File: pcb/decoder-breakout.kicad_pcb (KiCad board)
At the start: 2 copper layers, 18 parts, among them J1 SM04B-SRSS-TB_LF__SN_, J2 SM04B-SRSS-TB_LF__SN_, J3 TBL009-254-08GY-2GY, Q1 BSS138, Q2 BSS138, U1 LS7866-S

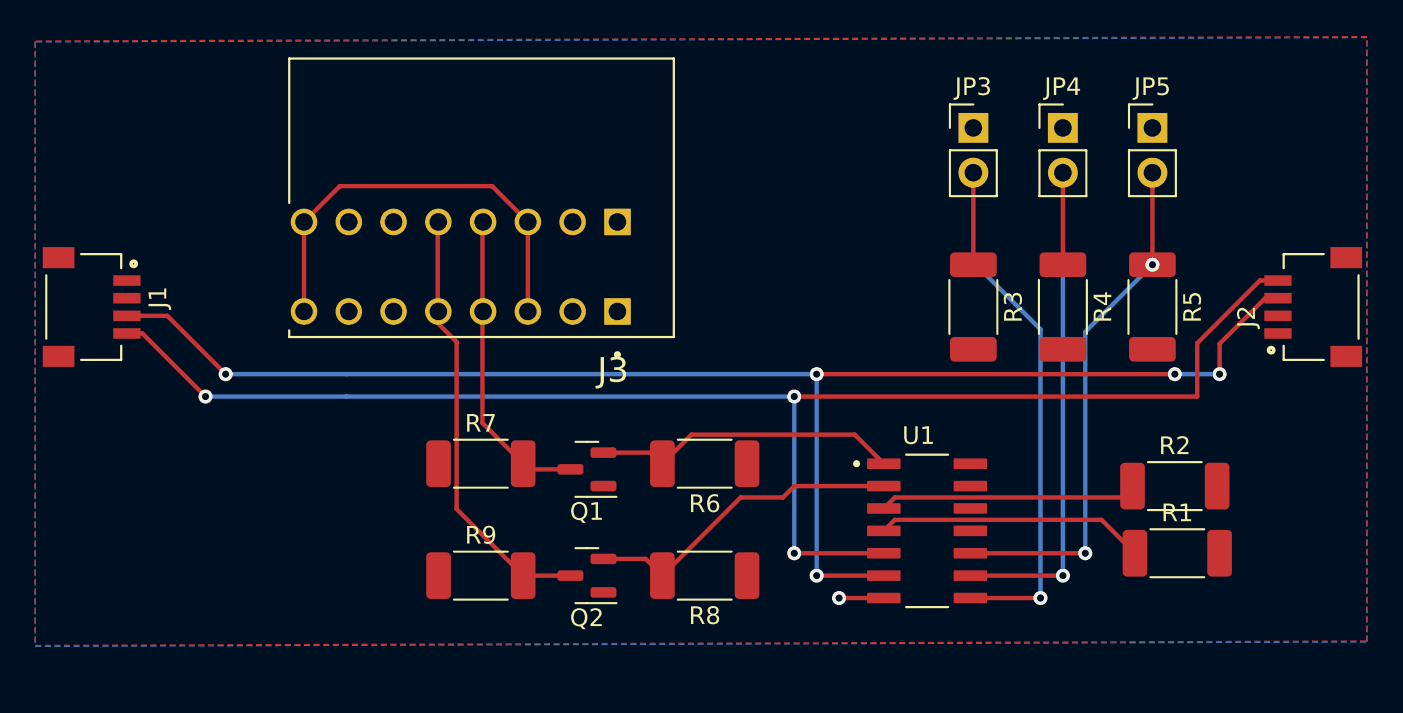
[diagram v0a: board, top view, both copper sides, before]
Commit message: add decoupling cap, mounting holes and board edges
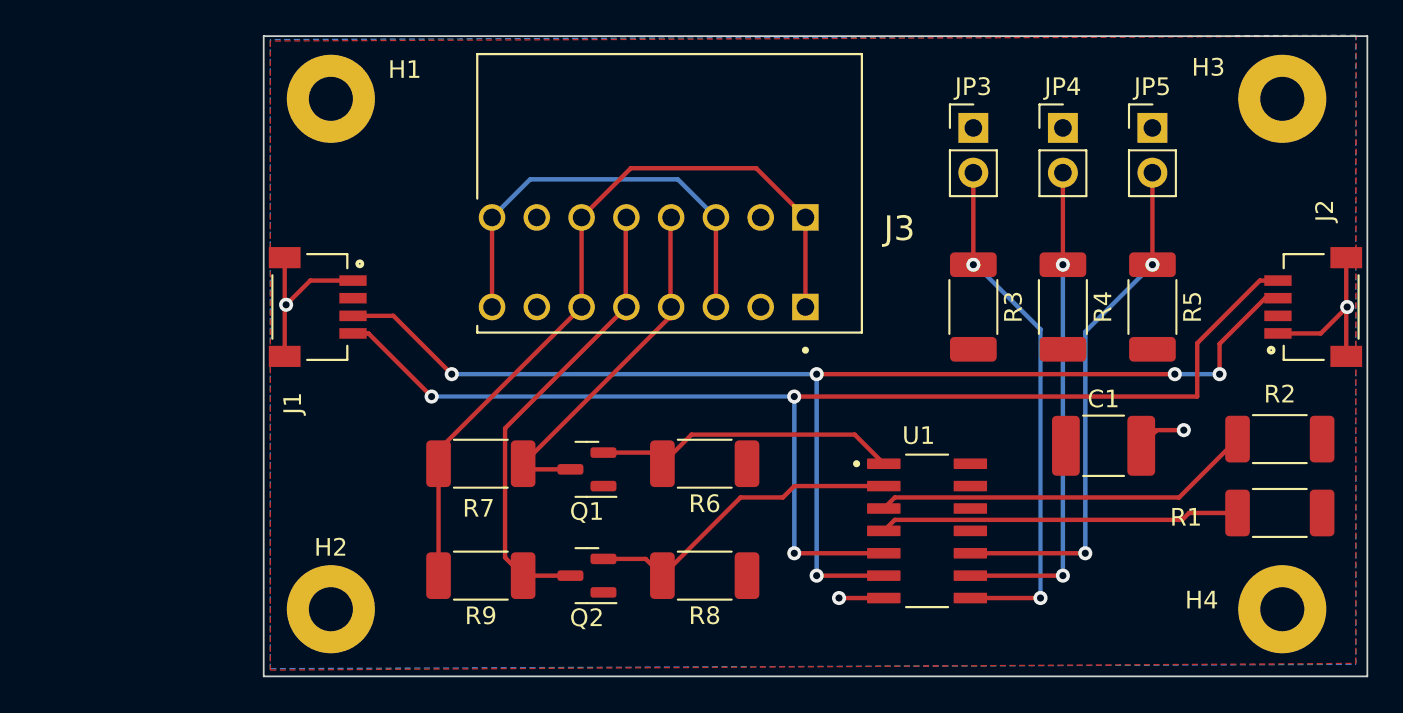
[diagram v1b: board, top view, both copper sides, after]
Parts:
- added C1: C, Capacitor_SMD:C_1812_4532Metric_Pad1.57x3.40mm_HandSolder, F.Cu at (142.0, 99.3)
- added H1: MountingHole, MountingHole:MountingHole_2.5mm_Pad, F.Cu at (98.2, 79.6)
- added H2: MountingHole, MountingHole:MountingHole_2.5mm_Pad, F.Cu at (98.2, 108.6)
- added H3: MountingHole, MountingHole:MountingHole_2.5mm_Pad, F.Cu at (152.1, 79.6)
- added H4: MountingHole, MountingHole:MountingHole_2.5mm_Pad, F.Cu at (152.1, 108.6)
- moved J1 12.8 mm to (99.4, 91.4)
- moved J3 10.7 mm to (125.1, 91.4)
- moved R2 6.53 mm to (152.0, 98.9)
- moved R1 6.25 mm to (152.0, 103.1)
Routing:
- net +5v: track 0.00 -> 43.8 mm
- net GND: track 2.54 -> 25.5 mm, vias 1 -> 4
- net Net-(U1-SDA): track 84.7 -> 71.9 mm
- net Net-(U1-SCL): track 85.3 -> 72.4 mm
- net Net-(U1-Z): track 14.6 -> 21.7 mm
- net Net-(U1-CE): track 15.3 -> 20.5 mm
- net Encoder_A: track 16.8 -> 20.3 mm
- net Encoder_B: track 24.1 -> 26.3 mm
- net Net-(JP4-B): vias 1 -> 2
- net Net-(JP3-B): vias 1 -> 2
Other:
- board outline added: 62.6 x 36.3 mm

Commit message: v0.1 as built
Update components, adjust layers, change directory, add elements

summary of diff --git  a/pcb/decoder-breakout.kicad_pcb b/pcb/decoder-breakout.kicad_pcb

- Update references and values for components Q2 and Q1
- Adjust various line strokes and polygon fills on F.SilkS and F.CrtYd layers
- Change model directory reference from KICAD6_3DMODEL_DIR to KICAD7_3DMODEL_DIR
- Add new resistor footprints with specified attributes and dimensions
- Include new segment and via connections on various layers for nets 2, 3, and 4
- Modify substrate dimensions in various segments
- Add text graphic on B.SilkS layer with project information
- Fix specific coordinate adjustments for overlapping geometries
- Add new via and segment elements to connect different parts of the circuit
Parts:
- added R10: 4.7k, Resistor_SMD:R_2010_5025Metric_Pad1.40x2.65mm_HandSolder, F.Cu at (99.8, 101.0)
- added R11: 4.7k, Resistor_SMD:R_2010_5025Metric_Pad1.40x2.65mm_HandSolder, F.Cu at (102.7, 85.5)
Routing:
- net Net-(U1-SCL): track 72.4 -> 77.3 mm
- net Net-(U1-SDA): track 71.9 -> 76.4 mm
- net VDD: track 0.00 -> 4.07 mm, vias 0 -> 2
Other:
- board text added: "cdint.com 472-1 v0.1 https://github.com/cdint/decoder-breakout"

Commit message: WIP replacing pin headers on PCB with 2x3 group
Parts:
- removed JP3, JP4, JP5: Jumper_2_Bridged, Connector_PinHeader_2.54mm:PinHeader_1x02_P2.54mm_Vertical
- added J4: Conn_02x03_Row_Letter_Last, Connector_PinHeader_2.54mm:PinHeader_2x03_P2.54mm_Vertical, F.Cu at (137.2, 80.0)

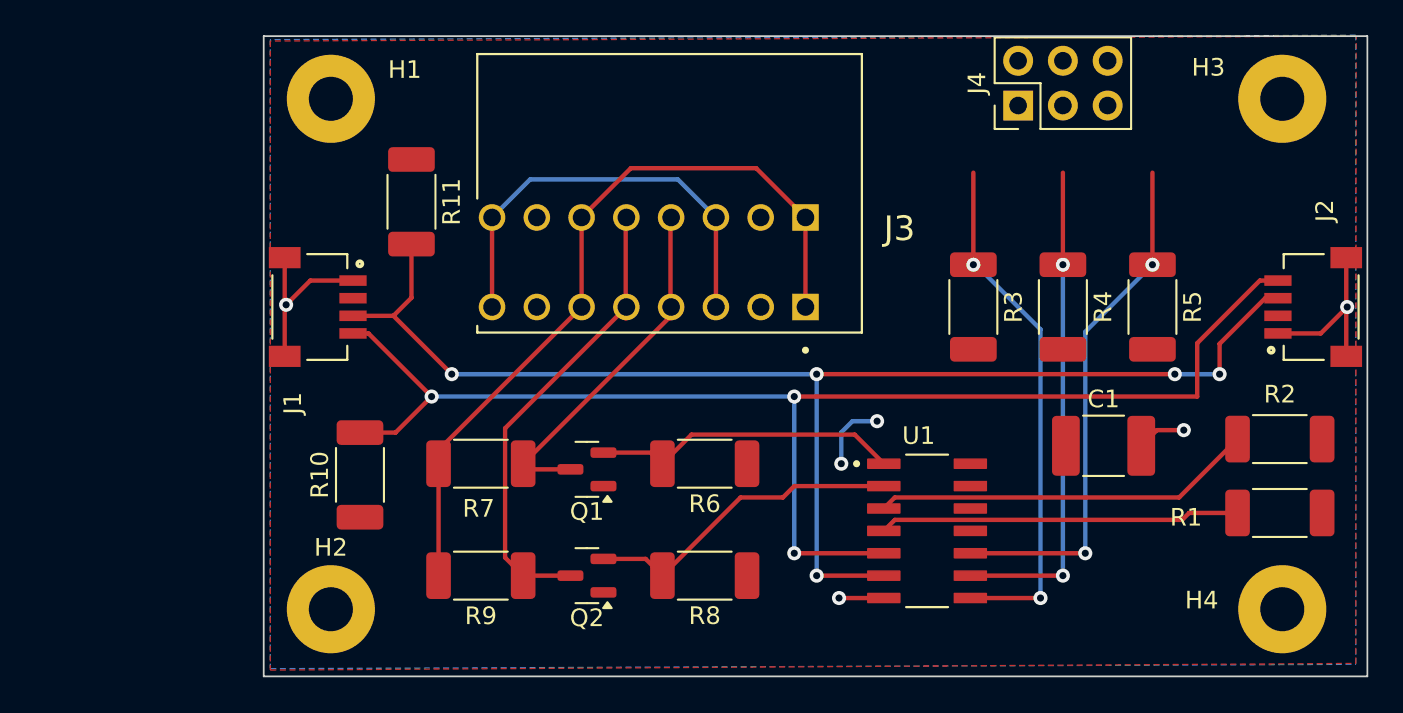
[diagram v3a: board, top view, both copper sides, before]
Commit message: v0.2 as built
- add silkscreen to terminal block
- group jumpers into 2x3 header
- move board edge so terminal block hangs over
- edit terminal block footprint locally to remove silkscreen box, so it does not error from being off board edge
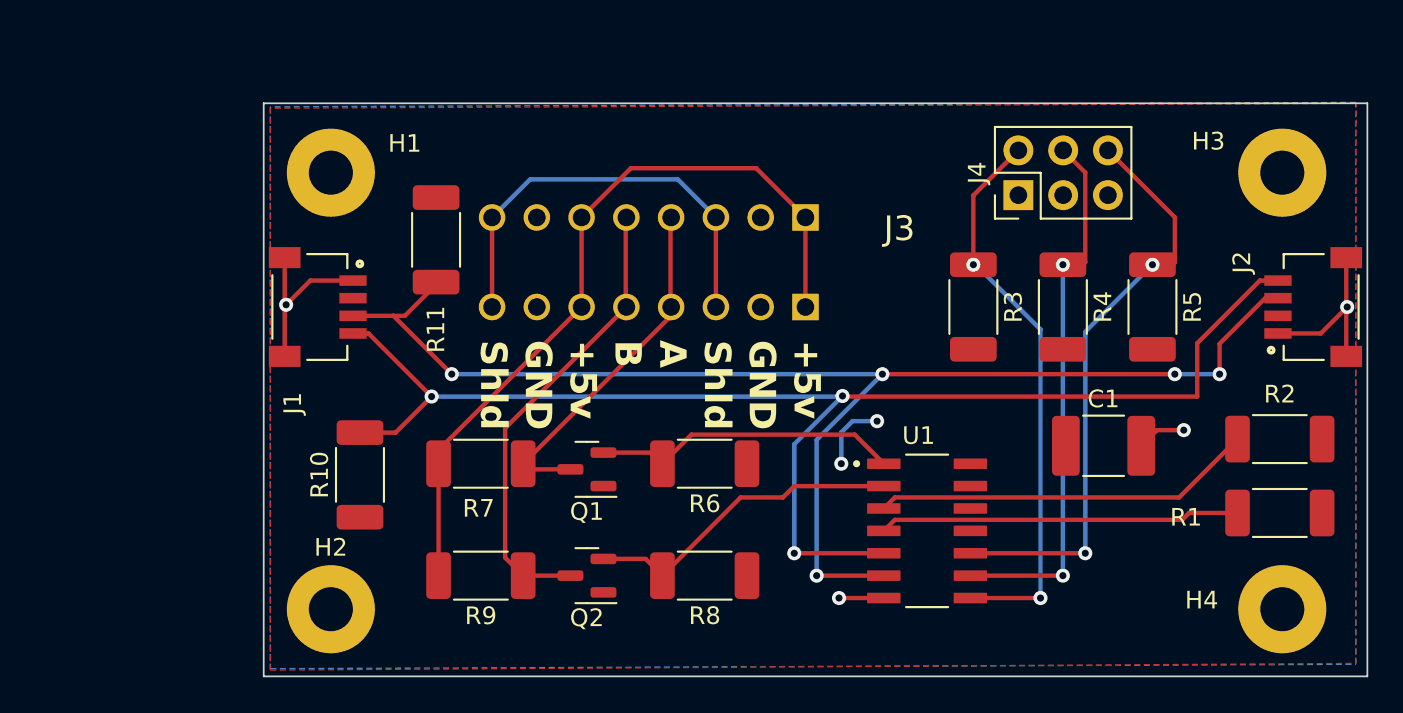
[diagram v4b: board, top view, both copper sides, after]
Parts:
- moved J4 5.09 mm to (137.2, 85.1)
- moved H1 4.19 mm to (98.2, 83.8)
- moved H3 4.19 mm to (152.1, 83.8)
- moved R11 2.57 mm to (104.1, 87.6)
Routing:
- net Net-(J4-Pin_2a): track 29.7 -> 33.7 mm
- net Net-(J4-Pin_3a): track 28.3 -> 31.2 mm
- net Net-(J4-Pin_1b): track 29.8 -> 32.2 mm
- net Net-(U1-SCL): track 77.3 -> 78.5 mm
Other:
- board size 62.6 x 36.3 mm -> 62.6 x 32.5 mm
- board text added: "+5v"
- board text added: "A"
- board text added: "B"
- board text added: "GND"
- board text added: "Shld"
- board text added: "cdint.com 472-1 v0.2 https://github.com/cdint/decoder-breakout"
- board text removed: "cdint.com 472-1 v0.1 https://github.com/cdint/decoder-breakout"

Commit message: v0.3 as built
- rotate J4 and add silkscreen
- move R10 and R11 to allow more room around J3
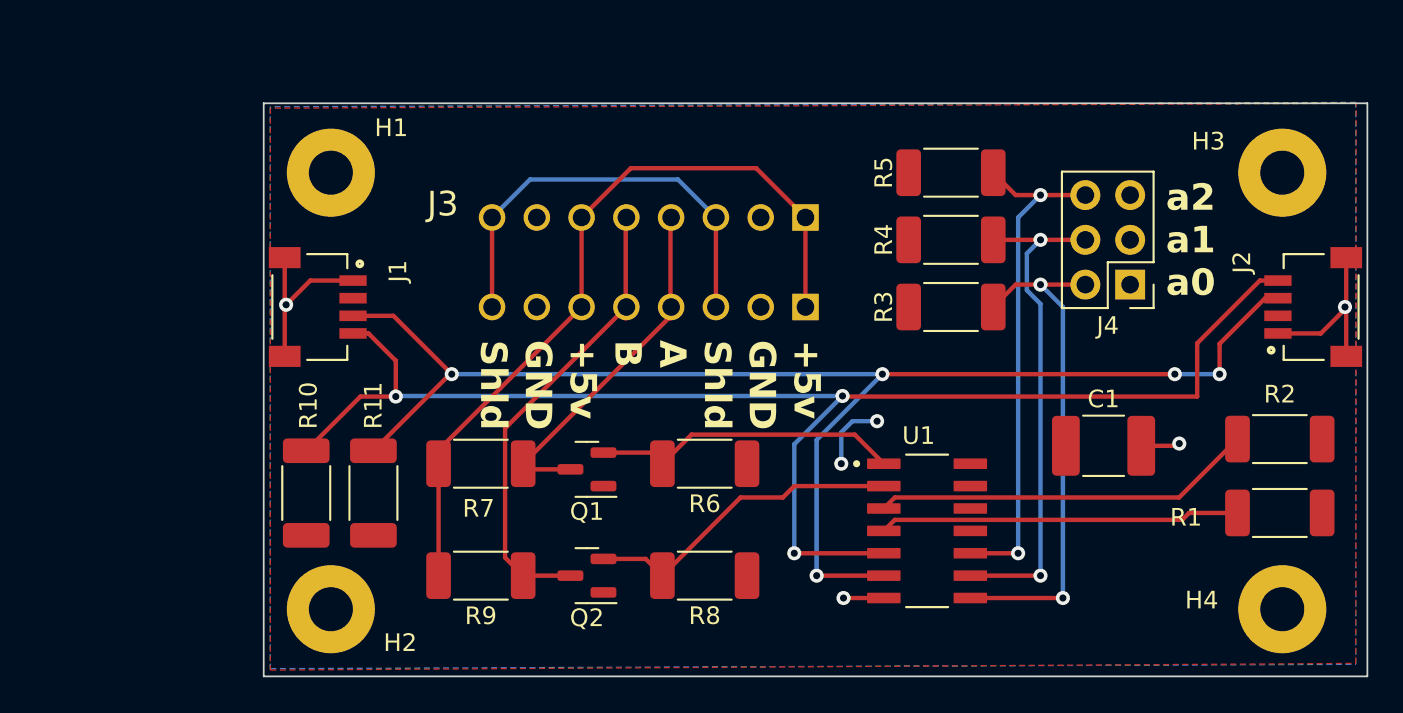
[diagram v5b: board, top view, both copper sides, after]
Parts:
- moved R11 14.8 mm to (100.6, 102.0), turned to 90 degrees
- moved R5 13.7 mm to (133.3, 83.8), turned to 180 degrees
- moved J4 8.12 mm to (143.5, 90.2), turned to 180 degrees
- moved R4 7.41 mm to (133.3, 87.6), turned to 180 degrees
- moved R10 3.22 mm to (96.8, 102.0)
- moved R3 1.27 mm to (133.3, 91.4), turned to 180 degrees
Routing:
- net Net-(J4-Pin_2a): track 33.7 -> 29.3 mm
- net Net-(U1-SDA): track 76.7 -> 79.7 mm
- net Net-(J4-Pin_1b): track 32.2 -> 29.3 mm
- net Net-(U1-SCL): track 78.5 -> 81.2 mm
- net Net-(J4-Pin_3a): track 31.2 -> 28.9 mm
- net Encoder_A: track 20.3 -> 19.3 mm
- net +5v: track 43.8 -> 43.0 mm
- net GND: track 25.6 -> 24.8 mm
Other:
- board text added: "a0"
- board text added: "a1"
- board text added: "a2"
- board text added: "cdint.com 472-1 v0.3 https://github.com/cdint/decoder-breakout"
- board text removed: "cdint.com 472-1 v0.2 https://github.com/cdint/decoder-breakout"
